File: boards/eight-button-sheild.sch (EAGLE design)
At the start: 9 parts, among them J4 ARDUINO_R3_SHIELD, SW1 BUTTON, SW2 BUTTON, SW3 BUTTON, SW4 BUTTON, SW5 BUTTON, SW6 BUTTON, SW7 BUTTON, SW8 BUTTON

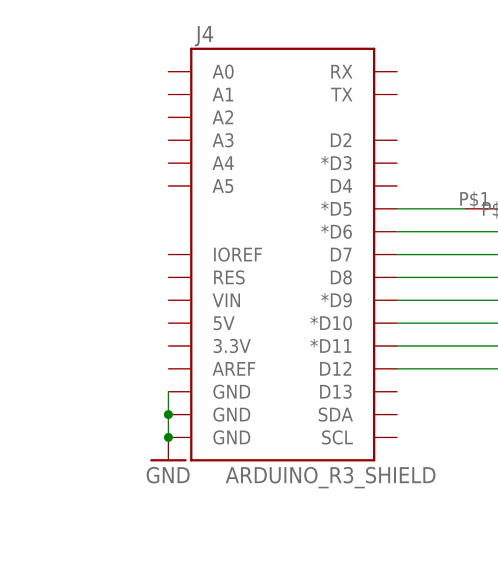
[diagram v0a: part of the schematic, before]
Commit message: added some breakout plated holes for A0-A6 and power pins to button board
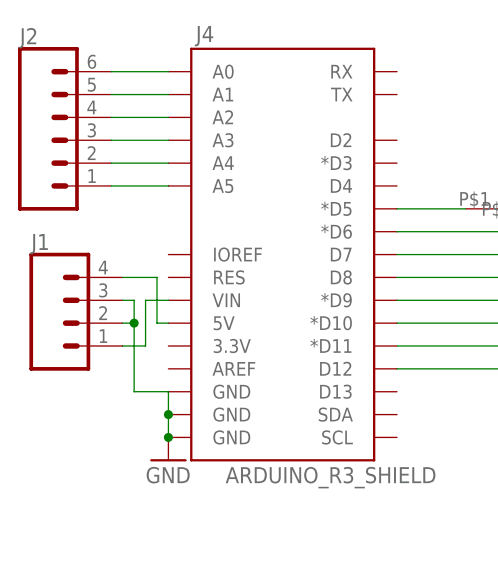
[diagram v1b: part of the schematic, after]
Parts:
- added J1: (no value), SparkFun-Connectors:CONN_04
- added J2: (no value), SparkFun-Connectors:CONN_06SILK_FEMALE_PTH
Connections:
- new net N$12: J2.2, J4.A4
- new net N$13: J2.3, J4.A3
- new net N$14: J2.4, J4.A2
- new net N$15: J2.5, J4.A1
- new net N$16: J2.6, J4.A0
- new net N$17: J1.1, J4.VIN
- new net N$18: J1.4, J4.5V
- new net N$9: J2.1, J4.A5
- net GND: now also J1.2, J1.3
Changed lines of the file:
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@@
 <part name="SW8" library="spietz-library" deviceset="BUTTON" device=""/>
 <part name="GND1" library="SparkFun-Aesthetics" deviceset="GND" device=""/>
+<part name="J1" library="SparkFun-Connectors" deviceset="CONN_04" device=""/>
+<part name="J2" library="SparkFun-Connectors" deviceset="CONN_06" device="SILK_FEMALE_PTH"/>
 </parts>
 <sheets>
@@
 <instance part="SW8" gate="G$1" x="200.66" y="78.74"/>
 <instance part="GND1" gate="1" x="81.28" y="68.58"/>
+<instance part="J1" gate="G$1" x="71.12" y="83.82"/>
+<instance part="J2" gate="G$1" x="69.85" y="104.14"/>
 </instances>
 <busses>
@@
 <junction x="81.28" y="73.66"/>
 <pinref part="J4" gate="G$1" pin="GND@2"/>
-<wire x1="81.28" y1="76.2" x2="81.28" y2="73.66" width="0.1524" layer="91"/>
 <pinref part="GND1" gate="1" pin="GND"/>
 <junction x="81.28" y="71.12"/>
-</segment>
-</net>
+<wire x1="81.28" y1="73.66" x2="81.28" y2="76.2" width="0.1524" layer="91"/>
+<wire x1="81.28" y1="76.2" x2="77.47" y2="76.2" width="0.1524" layer="91"/>
+<wire x1="77.47" y1="76.2" x2="77.47" y2="83.82" width="0.1524" layer="91"/>
+<pinref part="J1" gate="G$1" pin="2"/>
+<wire x1="77.47" y1="83.82" x2="76.2" y2="83.82" width="0.1524" layer="91"/>
+<pinref part="J1" gate="G$1" pin="3"/>
+<wire x1="76.2" y1="86.36" x2="77.47" y2="86.36" width="0.1524" layer="91"/>
+<wire x1="77.47" y1="86.36" x2="77.47" y2="83.82" width="0.1524" layer="91"/>
+<junction x="77.47" y="83.82"/>
+</segment>
+</net>
+<net name="N$9" class="0">
+<segment>
+<pinref part="J4" gate="G$1" pin="A5"/>
+<pinref part="J2" gate="G$1" pin="1"/>
+<wire x1="74.93" y1="99.06" x2="81.28" y2="99.06" width="0.1524" layer="91"/>
+</segment>
+</net>
+<net name="N$12" class="0">
+<segment>
+<pinref part="J4" gate="G$1" pin="A4"/>
+<pinref part="J2" gate="G$1" pin="2"/>
+<wire x1="74.93" y1="101.6" x2="81.28" y2="101.6" width="0.1524" layer="91"/>
+</segment>
+</net>
+<net name="N$13" class="0">
+<segment>
+<pinref part="J4" gate="G$1" pin="A3"/>
+<pinref part="J2" gate="G$1" pin="3"/>
+<wire x1="74.93" y1="104.14" x2="81.28" y2="104.14" width="0.1524" layer="91"/>
+</segment>
+</net>
+<net name="N$14" class="0">
+<segment>
+<pinref part="J4" gate="G$1" pin="A2"/>
+<pinref part="J2" gate="G$1" pin="4"/>
+<wire x1="74.93" y1="106.68" x2="81.28" y2="106.68" width="0.1524" layer="91"/>
+</segment>
+</net>
+<net name="N$15" class="0">
+<segment>
+<pinref part="J4" gate="G$1" pin="A1"/>
+<pinref part="J2" gate="G$1" pin="5"/>
+<wire x1="74.93" y1="109.22" x2="81.28" y2="109.22" width="0.1524" layer="91"/>
+</segment>
+</net>
+<net name="N$16" class="0">
+<segment>
+<pinref part="J4" gate="G$1" pin="A0"/>
+<pinref part="J2" gate="G$1" pin="6"/>
+<wire x1="74.93" y1="111.76" x2="81.28" y2="111.76" width="0.1524" layer="91"/>
+</segment>
+</net>
+<net name="N$17" class="0">
+<segment>
+<pinref part="J4" gate="G$1" pin="VIN"/>
+<wire x1="81.28" y1="86.36" x2="78.74" y2="86.36" width="0.1524" layer="91"/>
+<wire x1="78.74" y1="86.36" x2="78.74" y2="81.28" width="0.1524" layer="91"/>
+<pinref part="J1" gate="G$1" pin="1"/>
+<wire x1="78.74" y1="81.28" x2="76.2" y2="81.28" width="0.1524" layer="91"/>
+</segment>
+</net>
+<net name="N$18" class="0">
+<segment>
+<pinref part="J4" gate="G$1" pin="5V"/>
+<wire x1="81.28" y1="83.82" x2="80.01" y2="83.82" width="0.1524" layer="91"/>
+<wire x1="80.01" y1="83.82" x2="80.01" y2="88.9" width="0.1524" layer="91"/>
+<pinref part="J1" gate="G$1" pin="4"/>
+<wire x1="80.01" y1="88.9" x2="76.2" y2="88.9" width="0.1524" layer="91"/>
+</segment>
+</net>

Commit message: xyz stepper control
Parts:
- added J3: (no value), SparkFun-Connectors:CONN_09
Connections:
- net GND: now also J3.9
- net N$1: now also J3.1
- net N$10: now also J3.7
- net N$11: now also J3.8
- net N$4: now also J3.2
- net N$5: now also J3.3
- net N$6: now also J3.4
- net N$7: now also J3.5
- net N$8: now also J3.6
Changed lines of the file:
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@@
 <part name="J1" library="SparkFun-Connectors" deviceset="CONN_04" device=""/>
 <part name="J2" library="SparkFun-Connectors" deviceset="CONN_06" device="SILK_FEMALE_PTH"/>
+<part name="J3" library="SparkFun-Connectors" deviceset="CONN_09" device=""/>
+<part name="GND2" library="SparkFun-Aesthetics" deviceset="GND" device=""/>
 </parts>
 <sheets>
@@
 <instance part="J1" gate="G$1" x="71.12" y="83.82"/>
 <instance part="J2" gate="G$1" x="69.85" y="104.14"/>
+<instance part="J3" gate="J1" x="120.65" y="86.36" rot="R180"/>
+<instance part="GND2" gate="1" x="110.49" y="73.66"/>
 </instances>
 <busses>
@@
 <pinref part="J4" gate="G$1" pin="*D5"/>
 <pinref part="SW1" gate="G$1" pin="P$1"/>
-<wire x1="114.3" y1="96.52" x2="106.68" y2="96.52" width="0.1524" layer="91"/>
+<wire x1="114.3" y1="96.52" x2="110.49" y2="96.52" width="0.1524" layer="91"/>
+<pinref part="J3" gate="J1" pin="1"/>
+<wire x1="110.49" y1="96.52" x2="106.68" y2="96.52" width="0.1524" layer="91"/>
+<junction x="110.49" y="96.52"/>
 </segment>
 </net>
@@
 <pinref part="J4" gate="G$1" pin="*D6"/>
 <pinref part="SW2" gate="G$1" pin="P$1"/>
-<wire x1="106.68" y1="93.98" x2="125.73" y2="93.98" width="0.1524" layer="91"/>
+<wire x1="106.68" y1="93.98" x2="110.49" y2="93.98" width="0.1524" layer="91"/>
+<pinref part="J3" gate="J1" pin="2"/>
+<wire x1="110.49" y1="93.98" x2="125.73" y2="93.98" width="0.1524" layer="91"/>
+<junction x="110.49" y="93.98"/>
 </segment>
 </net>
@@
 <pinref part="J4" gate="G$1" pin="D7"/>
 <pinref part="SW3" gate="G$1" pin="P$1"/>
-<wire x1="106.68" y1="91.44" x2="135.89" y2="91.44" width="0.1524" layer="91"/>
+<wire x1="106.68" y1="91.44" x2="110.49" y2="91.44" width="0.1524" layer="91"/>
+<pinref part="J3" gate="J1" pin="3"/>
+<wire x1="110.49" y1="91.44" x2="135.89" y2="91.44" width="0.1524" layer="91"/>
+<junction x="110.49" y="91.44"/>
 </segment>
 </net>
@@
 <pinref part="J4" gate="G$1" pin="D8"/>
 <pinref part="SW4" gate="G$1" pin="P$1"/>
-<wire x1="106.68" y1="88.9" x2="144.78" y2="88.9" width="0.1524" layer="91"/>
+<wire x1="106.68" y1="88.9" x2="110.49" y2="88.9" width="0.1524" layer="91"/>
+<pinref part="J3" gate="J1" pin="4"/>
+<wire x1="110.49" y1="88.9" x2="144.78" y2="88.9" width="0.1524" layer="91"/>
+<junction x="110.49" y="88.9"/>
 </segment>
 </net>
@@
 <pinref part="J4" gate="G$1" pin="*D9"/>
 <pinref part="SW5" gate="G$1" pin="P$1"/>
-<wire x1="106.68" y1="86.36" x2="154.94" y2="86.36" width="0.1524" layer="91"/>
+<wire x1="106.68" y1="86.36" x2="110.49" y2="86.36" width="0.1524" layer="91"/>
+<pinref part="J3" gate="J1" pin="5"/>
+<wire x1="110.49" y1="86.36" x2="154.94" y2="86.36" width="0.1524" layer="91"/>
+<junction x="110.49" y="86.36"/>
 </segment>
 </net>
@@
 <pinref part="J4" gate="G$1" pin="*D10"/>
 <pinref part="SW6" gate="G$1" pin="P$1"/>
-<wire x1="106.68" y1="83.82" x2="165.1" y2="83.82" width="0.1524" layer="91"/>
+<wire x1="106.68" y1="83.82" x2="110.49" y2="83.82" width="0.1524" layer="91"/>
+<pinref part="J3" gate="J1" pin="6"/>
+<wire x1="110.49" y1="83.82" x2="165.1" y2="83.82" width="0.1524" layer="91"/>
+<junction x="110.49" y="83.82"/>
 </segment>
 </net>
@@
 <pinref part="SW7" gate="G$1" pin="P$1"/>
 <pinref part="J4" gate="G$1" pin="*D11"/>
-<wire x1="176.53" y1="81.28" x2="106.68" y2="81.28" width="0.1524" layer="91"/>
+<wire x1="176.53" y1="81.28" x2="110.49" y2="81.28" width="0.1524" layer="91"/>
+<pinref part="J3" gate="J1" pin="7"/>
+<wire x1="110.49" y1="81.28" x2="106.68" y2="81.28" width="0.1524" layer="91"/>
+<junction x="110.49" y="81.28"/>
 </segment>
 </net>
@@
 <pinref part="SW8" gate="G$1" pin="P$1"/>
 <pinref part="J4" gate="G$1" pin="D12"/>
-<wire x1="187.96" y1="78.74" x2="106.68" y2="78.74" width="0.1524" layer="91"/>
+<wire x1="187.96" y1="78.74" x2="110.49" y2="78.74" width="0.1524" layer="91"/>
+<pinref part="J3" gate="J1" pin="8"/>
+<wire x1="110.49" y1="78.74" x2="106.68" y2="78.74" width="0.1524" layer="91"/>
+<junction x="110.49" y="78.74"/>
 </segment>
 </net>
@@
 <junction x="77.47" y="83.82"/>
 </segment>
+<segment>
+<pinref part="J3" gate="J1" pin="9"/>
+<pinref part="GND2" gate="1" pin="GND"/>
+</segment>
 </net>
